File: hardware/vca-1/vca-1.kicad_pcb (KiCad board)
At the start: 2 copper layers, 40 x 100 mm, 47 parts, among them J1 LIN CV IN, J2 AUDIO IN, J3 OUT, J4 LIN CV IN, J5 AUDIO IN, J6 OUT, J7 Conn_02x05_Odd_Even, Q1 BC557, Q2 BC557, U1 TL074, U2 LM13700

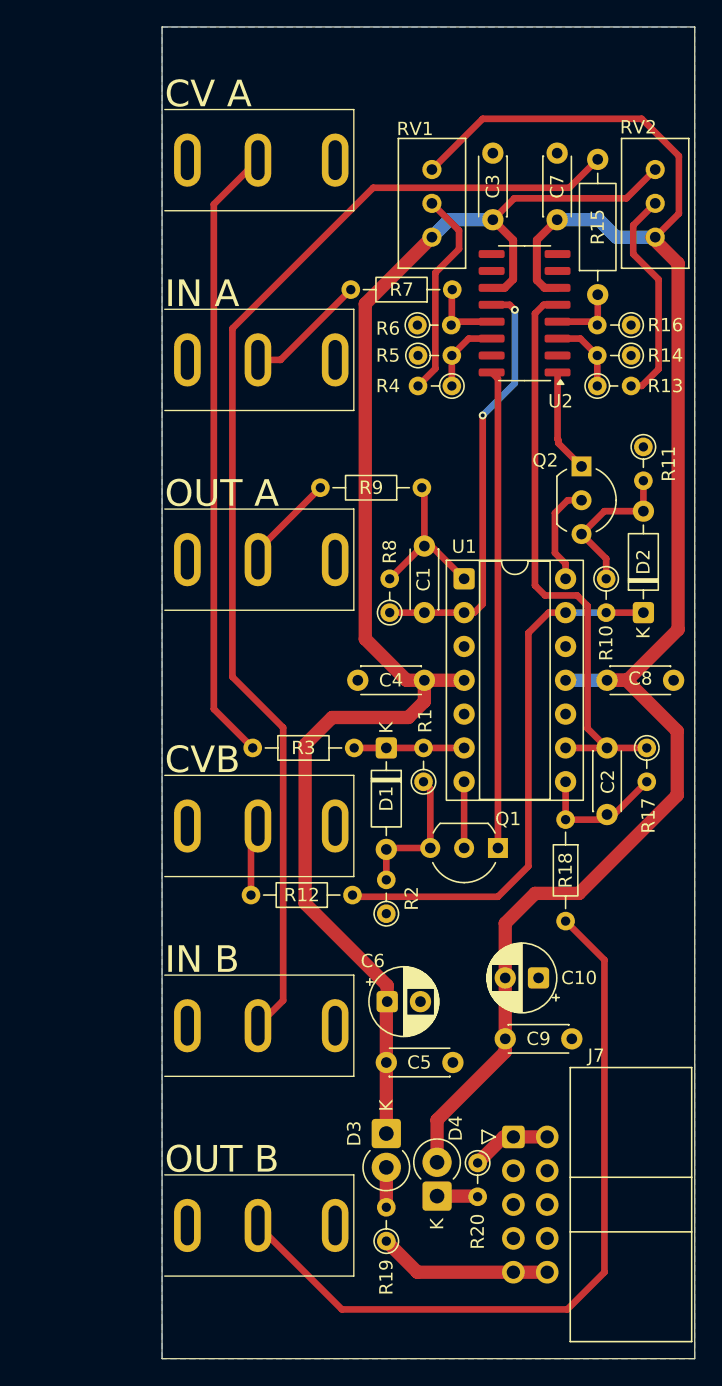
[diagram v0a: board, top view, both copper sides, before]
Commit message: Added a level pot on the audio inputs, v1.1
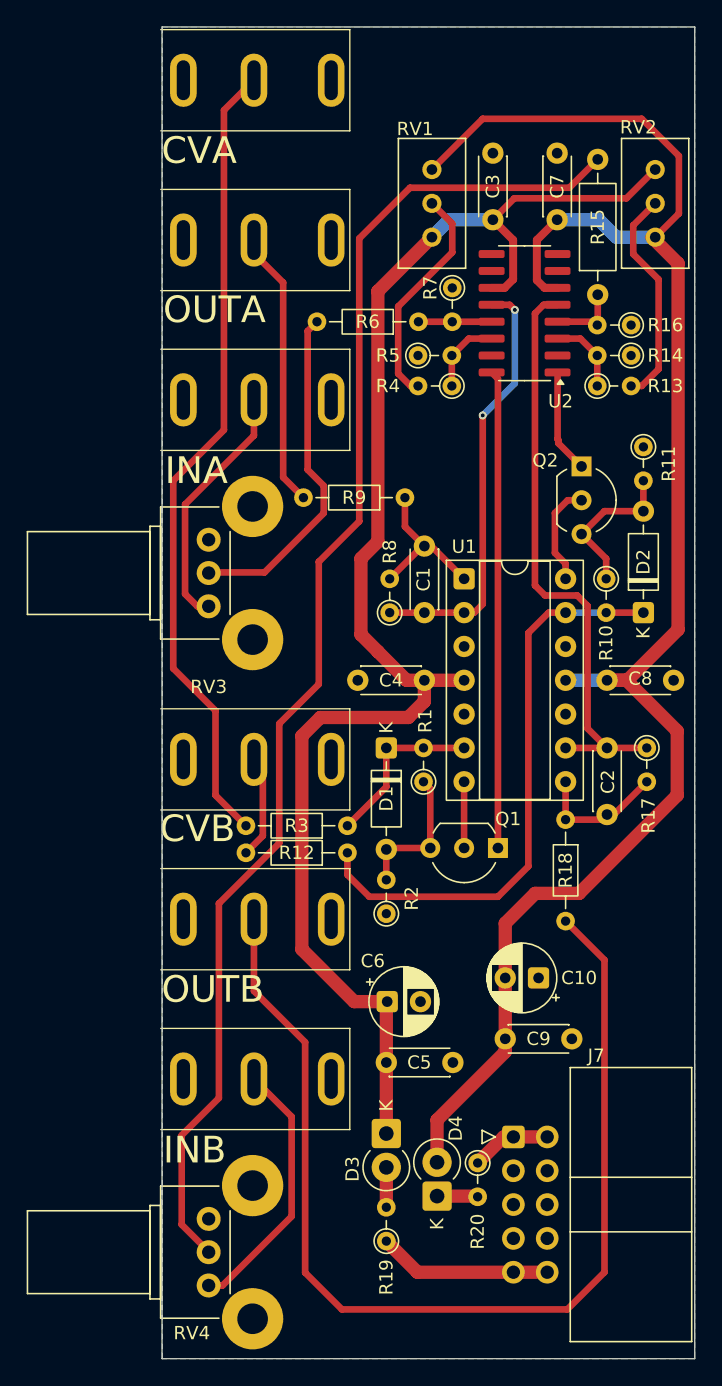
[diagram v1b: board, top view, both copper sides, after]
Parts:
- added RV3: 100k, Potentiometer_THT:Potentiometer_Bourns_PTV09A-2_Single_Horizontal, F.Cu at (103.5, 88.5)
- added RV4: 100k, Potentiometer_THT:Potentiometer_Bourns_PTV09A-2_Single_Horizontal, F.Cu at (103.5, 139.5)
- R17, R8: value 47k -> 49k9
- moved J3 24.0 mm to (101.6, 66.0)
- moved J6 23.0 mm to (101.6, 117.0)
- moved J1 6.01 mm to (101.6, 54.0)
- moved R3 5.86 mm to (113.9, 110.0)
- moved J4 5.01 mm to (101.6, 105.0)
- moved J5 4.01 mm to (101.6, 129.0)
- moved R7 3.83 mm to (121.8, 69.6), turned to -90 degrees
- moved R6 3.50 mm to (119.3, 72.1)
- moved R12 3.20 mm to (113.9, 112.0)
- moved J2 3.01 mm to (101.6, 78.0)
- moved R9 1.47 mm to (118.2, 85.3)
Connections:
- R15 pad 2: Net-(J5-PadT) -> Net-(R15-Pad2)
- R6 pad 2: Net-(J2-PadT) -> Net-(R6-Pad2)
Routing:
- net Net-(R15-Pad2): track 0.00 -> 102.8 mm
- net Net-(J5-PadT): track 87.4 -> 19.9 mm
- net Net-(R6-Pad2): track 0.00 -> 25.6 mm
- net Net-(J6-PadT): track 57.4 -> 80.5 mm
- net Net-(J1-PadT): track 46.7 -> 60.8 mm
- net Net-(J3-PadT): track 7.34 -> 19.9 mm
- net Net-(J2-PadT): track 9.16 -> 18.9 mm
- net Net-(D1-K): track 8.25 -> 12.9 mm
- net Net-(D2-K): track 41.0 -> 43.7 mm
- net +12V: track 110.5 -> 112.9 mm
- net Net-(J4-PadT): track 5.40 -> 7.82 mm
- net Net-(R4-Pad2): track 15.8 -> 17.0 mm
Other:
- board text added: "CVA"
- board text added: "INA"
- board text added: "INB"
- board text added: "OUTA"
- board text added: "OUTB"
- board text added: "idyllm CC BY-SA 4.0 v1.1.20250620"
- board text removed: "CV A"
- board text removed: "IN A"
- board text removed: "IN B"
- board text removed: "OUT A"
- board text removed: "OUT B"
- board text removed: "idyllm CC BY-SA 4.0 v1.0.20250619"
